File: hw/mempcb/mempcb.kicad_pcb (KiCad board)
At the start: 4 copper layers, 0 parts

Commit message: BROKEN hw/mempcb/: initial component placement; up-side down bus conn.
The RC6502 bus connector is upside-down compared to normal boards, with the
pins going the wrong direction when looking at the component side as
compared with all other RC6502 boards. This must be fixed because otherwise
it's almost certain to lead to someone inserting a board into the backplane
backwards.
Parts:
- added BUSPWR_EN1: 0.1" 1x2, Connector_PinHeader_2.54mm:PinHeader_1x02_P2.54mm_Vertical, F.Cu at (96.5, 53.0)
- added HIGH1: 0.1" 1x4, Connector_PinHeader_2.54mm:PinHeader_1x04_P2.54mm_Vertical, F.Cu at (118.1, 139.4)
- added J1: RC6502_Bus, Connector_PinHeader_2.54mm:PinHeader_1x39_P2.54mm_Vertical, F.Cu at (82.5, 51.8)
- added J2: 0.1" 2x25, Connector_PinHeader_2.54mm:PinHeader_2x25_P2.54mm_Vertical, F.Cu at (174.0, 54.3)
- added LOW1: 0.1" 1x4, Connector_PinHeader_2.54mm:PinHeader_1x04_P2.54mm_Vertical, F.Cu at (110.5, 139.4)
- added PULLDOWN1: 0.1" 1x4, Connector_PinHeader_2.54mm:PinHeader_1x04_P2.54mm_Vertical, F.Cu at (94.0, 139.4)
- added PULLUP1: 0.1" 1x4, Connector_PinHeader_2.54mm:PinHeader_1x04_P2.54mm_Vertical, F.Cu at (134.6, 139.4)
- added PWR1: JST-XH, Connector_JST:JST_XH_B2B-XH-A_1x02_P2.50mm_Vertical, F.Cu at (148.5, 54.3)
- added PWR2: JST-XH, Connector_JST:JST_XH_B2B-XH-A_1x02_P2.50mm_Vertical, F.Cu at (138.4, 54.3)
- added R1: R, Resistor_THT:R_Axial_DIN0207_L6.3mm_D2.5mm_P10.16mm_Horizontal, F.Cu at (131.4, 138.1)
- added R2: R, Resistor_THT:R_Axial_DIN0207_L6.3mm_D2.5mm_P10.16mm_Horizontal, F.Cu at (131.4, 141.3)
- added R3: R, Resistor_THT:R_Axial_DIN0207_L6.3mm_D2.5mm_P10.16mm_Horizontal, F.Cu at (131.4, 144.5)
- added R4: R, Resistor_THT:R_Axial_DIN0207_L6.3mm_D2.5mm_P10.16mm_Horizontal, F.Cu at (131.4, 147.7)
- added R5: R, Resistor_THT:R_Axial_DIN0207_L6.3mm_D2.5mm_P10.16mm_Horizontal, F.Cu at (97.1, 138.1)
- added R6: R, Resistor_THT:R_Axial_DIN0207_L6.3mm_D2.5mm_P10.16mm_Horizontal, F.Cu at (97.1, 141.3)
- added R7: R, Resistor_THT:R_Axial_DIN0207_L6.3mm_D2.5mm_P10.16mm_Horizontal, F.Cu at (97.1, 144.5)
- added R8: R, Resistor_THT:R_Axial_DIN0207_L6.3mm_D2.5mm_P10.16mm_Horizontal, F.Cu at (97.1, 147.7)
- added U3: JEDEC_DIP32_RAM, Package_DIP:DIP-32_W15.24mm_Socket_LongPads, F.Cu at (110.5, 61.9)
- added U4: 74LS138, Package_DIP:DIP-16_W7.62mm_Socket_LongPads, F.Cu at (110.5, 112.7)
- added W1: RC6502_Bus, Connector_PinHeader_2.54mm:PinHeader_1x39_P2.54mm_Vertical, F.Cu at (87.6, 51.8)
- added W2_1: 0.1" 1x25, Connector_PinHeader_2.54mm:PinHeader_1x25_P2.54mm_Vertical, F.Cu at (166.4, 54.3)
- added W2_2: 0.1" 1x25, Connector_PinHeader_2.54mm:PinHeader_1x25_P2.54mm_Vertical, F.Cu at (161.3, 54.3)
- added W3_1: 0.1" 1x16, Connector_PinHeader_2.54mm:PinHeader_1x16_P2.54mm_Vertical, F.Cu at (100.3, 61.9)
- added W3_2: 0.1" 1x16, Connector_PinHeader_2.54mm:PinHeader_1x16_P2.54mm_Vertical, F.Cu at (135.9, 61.9)
- added W4_1: 0.1" 1x8, Connector_PinHeader_2.54mm:PinHeader_1x08_P2.54mm_Vertical, F.Cu at (100.3, 112.7)
- added W4_2: 0.1" 1x8, Connector_PinHeader_2.54mm:PinHeader_1x08_P2.54mm_Vertical, F.Cu at (128.3, 112.7)
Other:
- board outline added: 100 x 100 mm

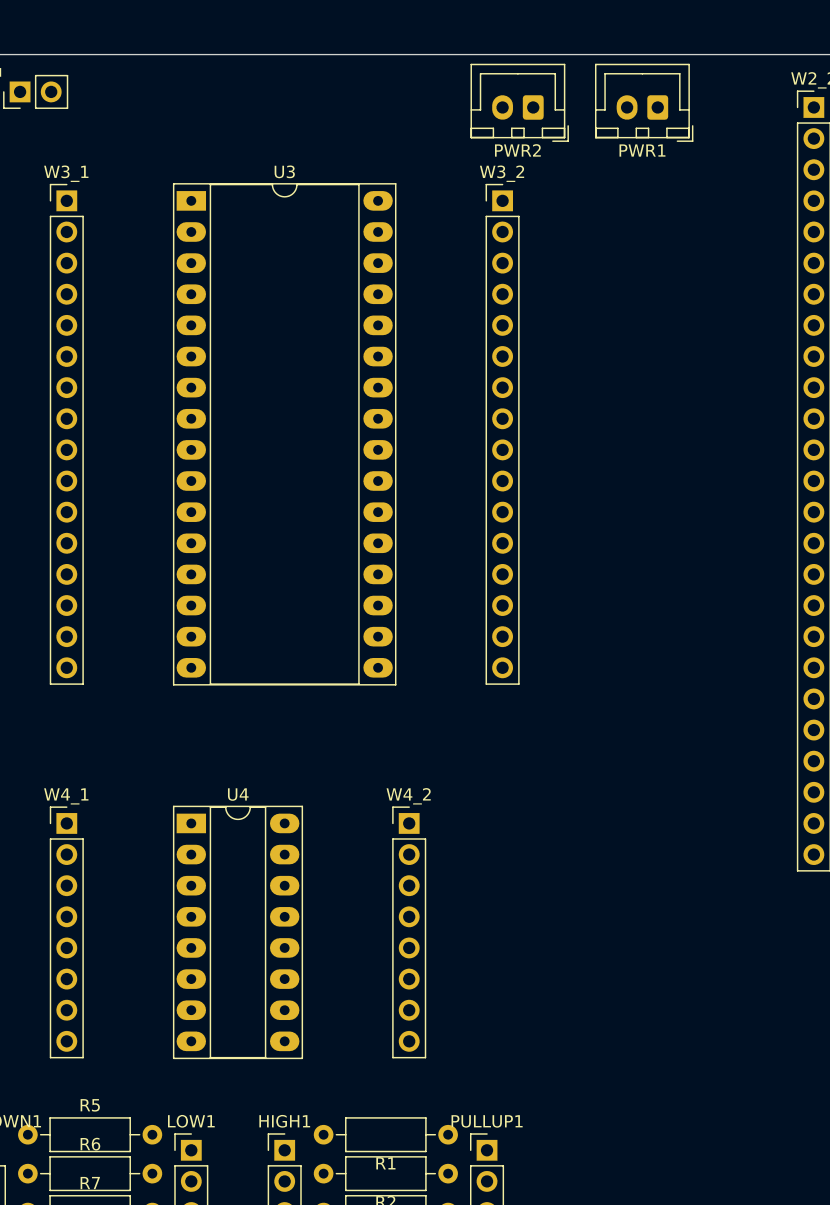
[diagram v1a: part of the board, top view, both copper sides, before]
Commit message: BROKEN hw/mempcb/: add another DIP16 and bypass caps
For 6502 systems, qualifying the RAM write line with Φ2 is essential for
reliable operation. If a 74'138 is used for address decoding, we will need
some separate gates for that, so add another socket for those.

The RC6502 bus connector is still backwards.
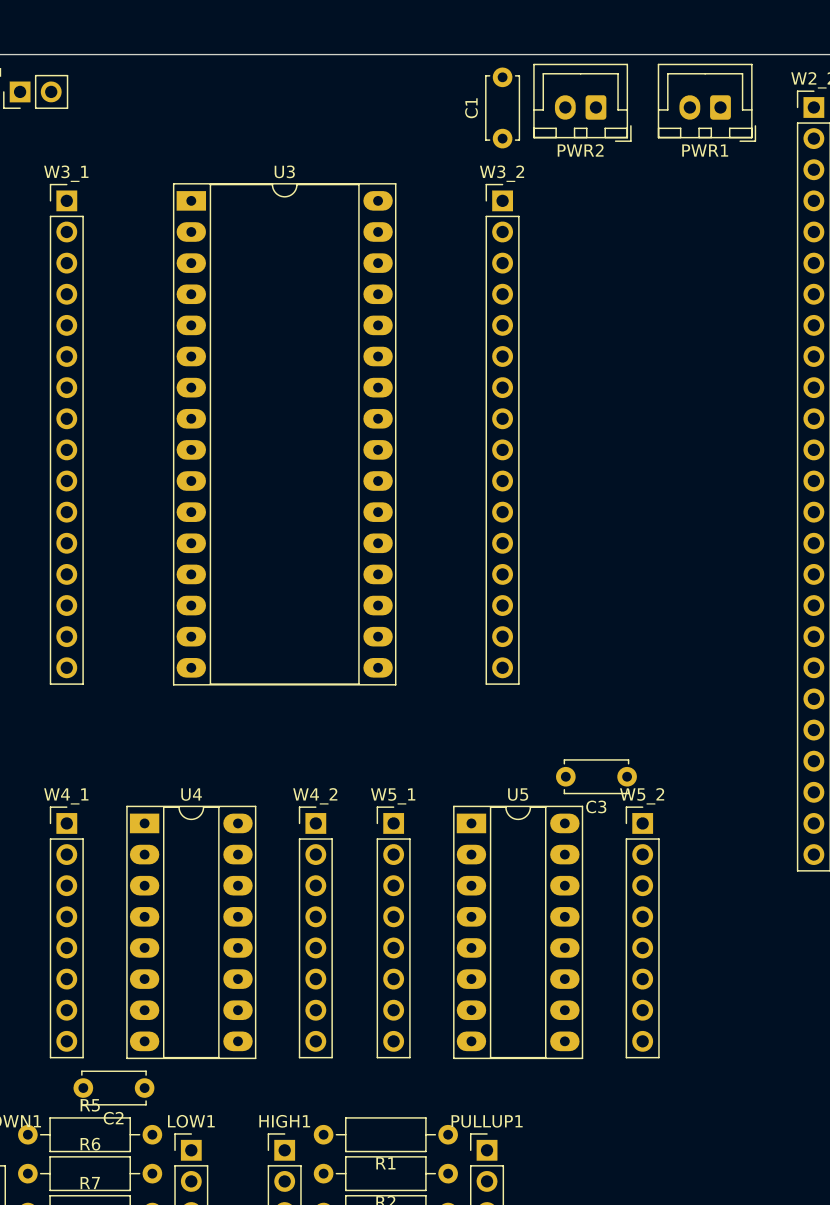
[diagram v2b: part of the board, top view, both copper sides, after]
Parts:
- added C1: .1μF, Capacitor_THT:C_Disc_D5.0mm_W2.5mm_P5.00mm, F.Cu at (135.9, 56.9)
- added C2: .1μF, Capacitor_THT:C_Disc_D5.0mm_W2.5mm_P5.00mm, F.Cu at (106.7, 134.3)
- added C3: .1μF, Capacitor_THT:C_Disc_D5.0mm_W2.5mm_P5.00mm, F.Cu at (146.0, 108.9)
- added U5: 74LS138, Package_DIP:DIP-16_W7.62mm_Socket_LongPads, F.Cu at (133.3, 112.7)
- added W5_1: 0.1" 1x8, Connector_PinHeader_2.54mm:PinHeader_1x08_P2.54mm_Vertical, F.Cu at (127.0, 112.7)
- added W5_2: 0.1" 1x8, Connector_PinHeader_2.54mm:PinHeader_1x08_P2.54mm_Vertical, F.Cu at (147.3, 112.7)
- moved W4_2 7.62 mm to (120.6, 112.7)
- moved PWR1 5.12 mm to (153.7, 54.3)
- moved PWR2 5.12 mm to (143.5, 54.3)
- moved U4 3.81 mm to (106.7, 112.7)

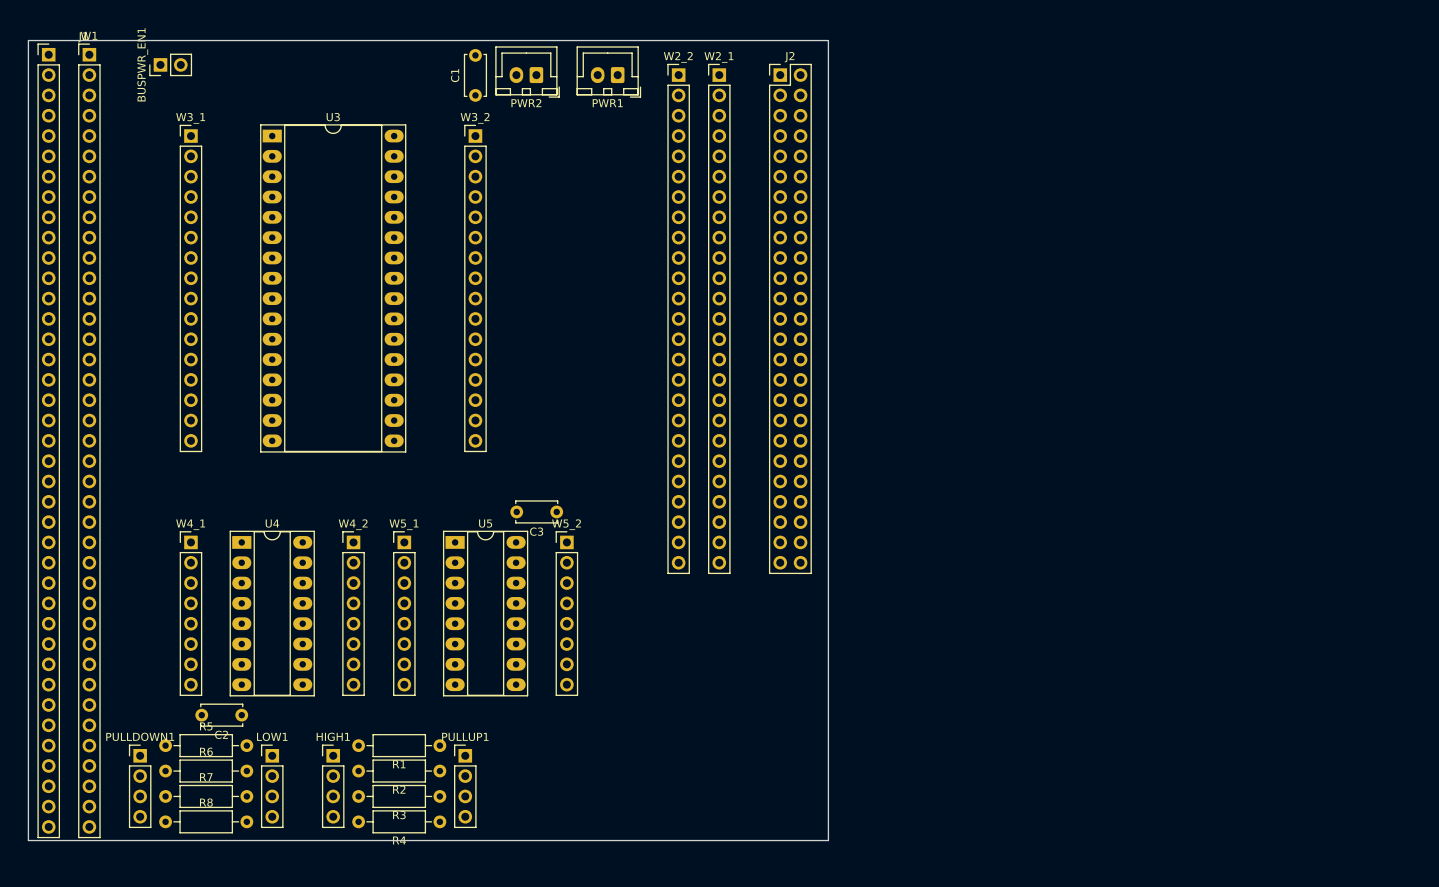
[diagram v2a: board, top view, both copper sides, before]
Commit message: WIP hw/mempcb/ PCB: Intermediate stage of moving to vertical orientation
- RC6502 bus connector moved to bottom edge.
- 2×25 expansion bus connector at upper left.
- Memory chip vertical at top centre.
- All other parts off-board temporarily.

This commit is kept to be able to show the idea and in case we want to
try moving in a different diretion from this point.
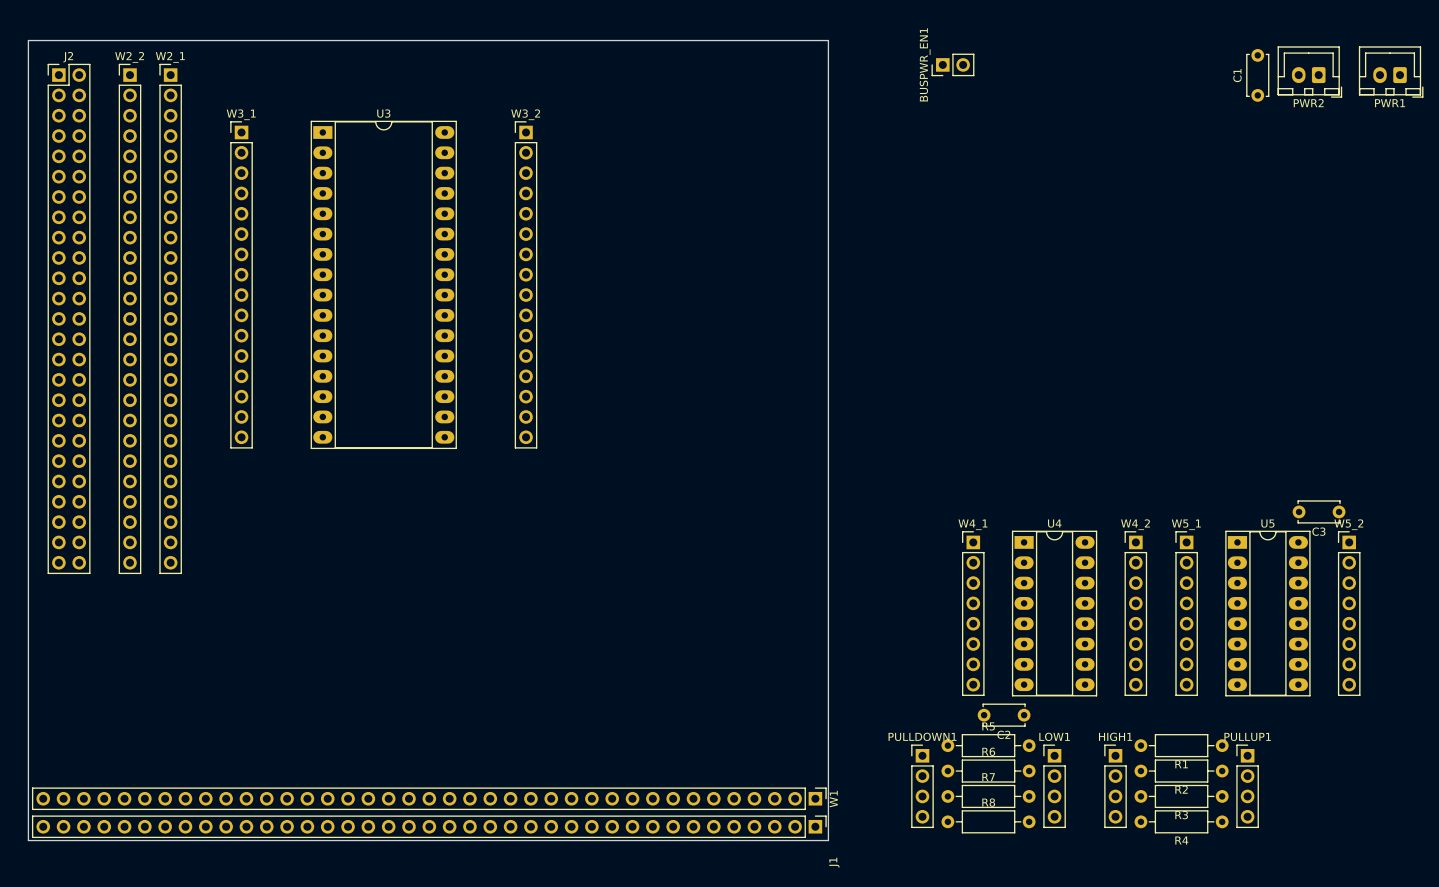
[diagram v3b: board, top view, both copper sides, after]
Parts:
- moved J1 136.0 mm to (178.4, 148.3), turned to 270 degrees
- moved W1 129.9 mm to (178.4, 144.8), turned to 270 degrees
- moved C3 97.8 mm to (243.8, 108.9)
- moved W4_1 97.8 mm to (198.1, 112.7)
- moved BUSPWR_EN1 97.8 mm to (194.3, 53.0)
- moved C2 97.8 mm to (204.5, 134.3)
- moved LOW1 97.8 mm to (208.3, 139.4)
- moved R5 97.8 mm to (194.9, 138.1)
- moved R6 97.8 mm to (194.9, 141.3)
- moved R7 97.8 mm to (194.9, 144.5)
- moved R8 97.8 mm to (194.9, 147.7)
- moved U4 97.8 mm to (204.5, 112.7)
- moved W4_2 97.8 mm to (218.4, 112.7)
- moved W5_1 97.8 mm to (224.8, 112.7)
- moved C1 97.8 mm to (233.7, 56.9)
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
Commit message: hw/mempcb/ PCB: Vertical memory; still horizontal logic
- RC6502 bus connector has the pin orientation fixed. It's also moved to
  bottom edge, because it's easier to think about the board in context when
  viewed in the "normal" orientation in which it's inserted into the bus.

- DIP-32 (memory) vertical at top centre. This seems to greatly reduce the
  problem of crossover of signals from the RC6502 bus. If a ZIF socket is
  used, its lever will stick out the top of the card, which is probably
  better. We also move the wire-wrap pins outward a bit on the pins 16-32
  side to make room for the bypass cap between the pins and the body of a
  ZIF socket; this gives maximal shortening of the distance through this
  between power and ground, and keeps it generally out of the way of any
  wire wrap.going around the socket.

- 2×25 expansion bus connector is now vertical at the upper left, with the
  wire-wrap pins parallel to it. This is probably the optimal place and
  orientation in relation to the DIP-32 for connectivity, bringing at least
  12 pins that must be hand-connected (A7-A0, D0-D3, GND) close together.

- DIP-16 logic sockets for decoding and qualification are horizontal below
  the DIP-32, with pin 1 lower left. For a '132 this puts the inputs on the
  RC6502 bus side, and the outputs mainly on the DIP-32 side, and right
  DIP-16 is fairly conveniently close to the address lines that we'll
  probably be decoding. The left one is above signal lines such as clock
  that we'd use for qualification.

- Power to/from off-board goes directly under the 2×25 header, which keeps
  together all cables going off board.

- Bus power jumper is almost directly above the bus power pin, which is at
  least eminently logical. Above it are the two bypass caps for the
  DIP-16s, which nestle between the two sockets.

- Pull-ups/-downs fit nicely in the lower right.

- Lots of space is available for prototyping aria in the upper right.

Some of the things here don't seem to 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
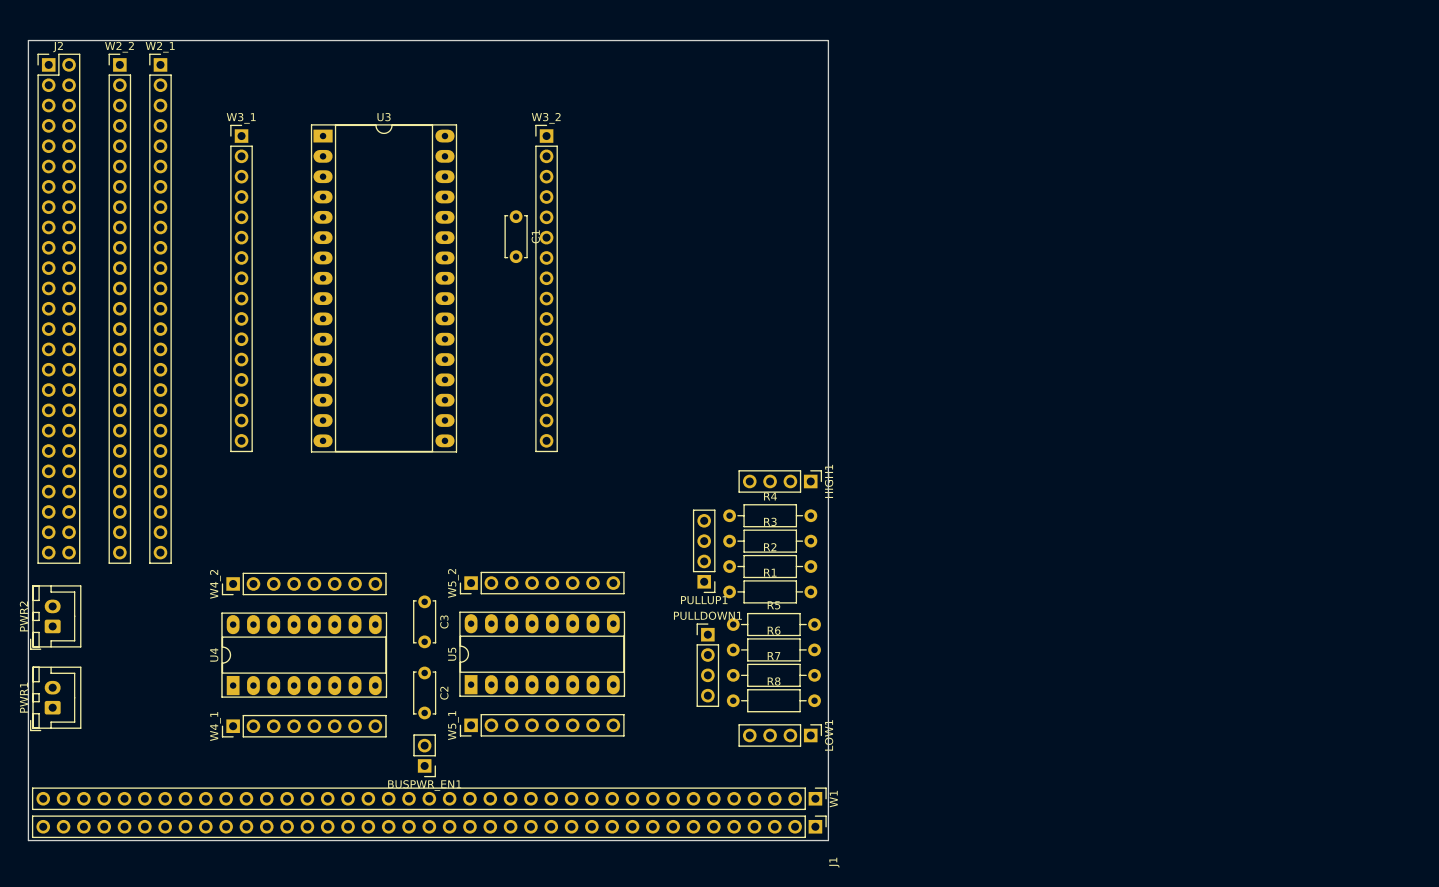
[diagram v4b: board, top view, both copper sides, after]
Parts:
- moved PWR1 186.1 mm to (83.0, 133.4), turned to 90 degrees
- moved PWR2 172.6 mm to (83.0, 123.2), turned to 90 degrees
- moved C3 114.9 mm to (129.5, 120.2), turned to 270 degrees
- moved W4_2 113.0 mm to (105.6, 117.9), turned to 90 degrees
- moved W5_2 109.9 mm to (135.3, 117.8), turned to 90 degrees
- moved BUSPWR_EN1 109.0 mm to (129.5, 140.7), turned to 180 degrees
- moved U4 100.5 mm to (105.6, 130.6), turned to 90 degrees
- moved U5 97.4 mm to (135.3, 130.5), turned to 90 degrees
- moved W4_1 95.3 mm to (105.6, 135.7), turned to 90 degrees
- moved C1 93.9 mm to (141.0, 72.0), turned to 270 degrees
- moved W5_1 92.3 mm to (135.3, 135.6), turned to 90 degrees
- moved C2 75.1 mm to (129.5, 129.1), turned to 270 degrees
- moved R4 72.5 mm to (167.6, 109.4), turned to 0 degrees
- moved PULLUP1 71.3 mm to (164.5, 117.7), turned to 180 degrees
- moved R3 69.4 mm to (167.6, 112.6), turned to 0 degrees
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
